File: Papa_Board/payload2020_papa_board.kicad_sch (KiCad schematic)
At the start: 18 parts, among them J2 Conn_01x05, J3 Conn_01x05_Female, J4 Conn_01x05, J5 M80-5000642, J6 M80-5000642, U11 FPF2125

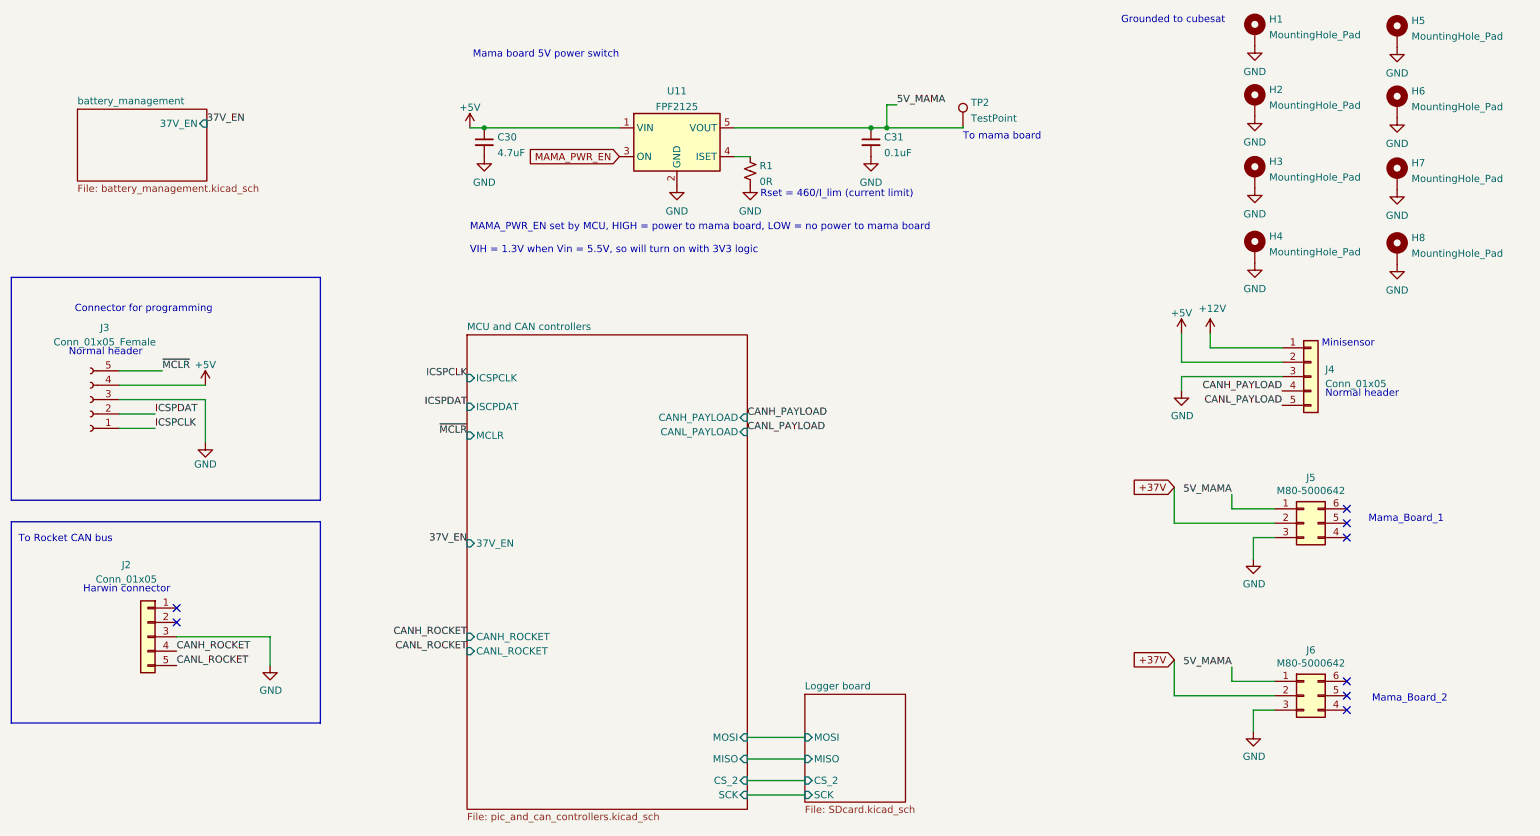
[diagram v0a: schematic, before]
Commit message: Address Jack's schematic review, still need to update PCB layout and figure out CAN connections
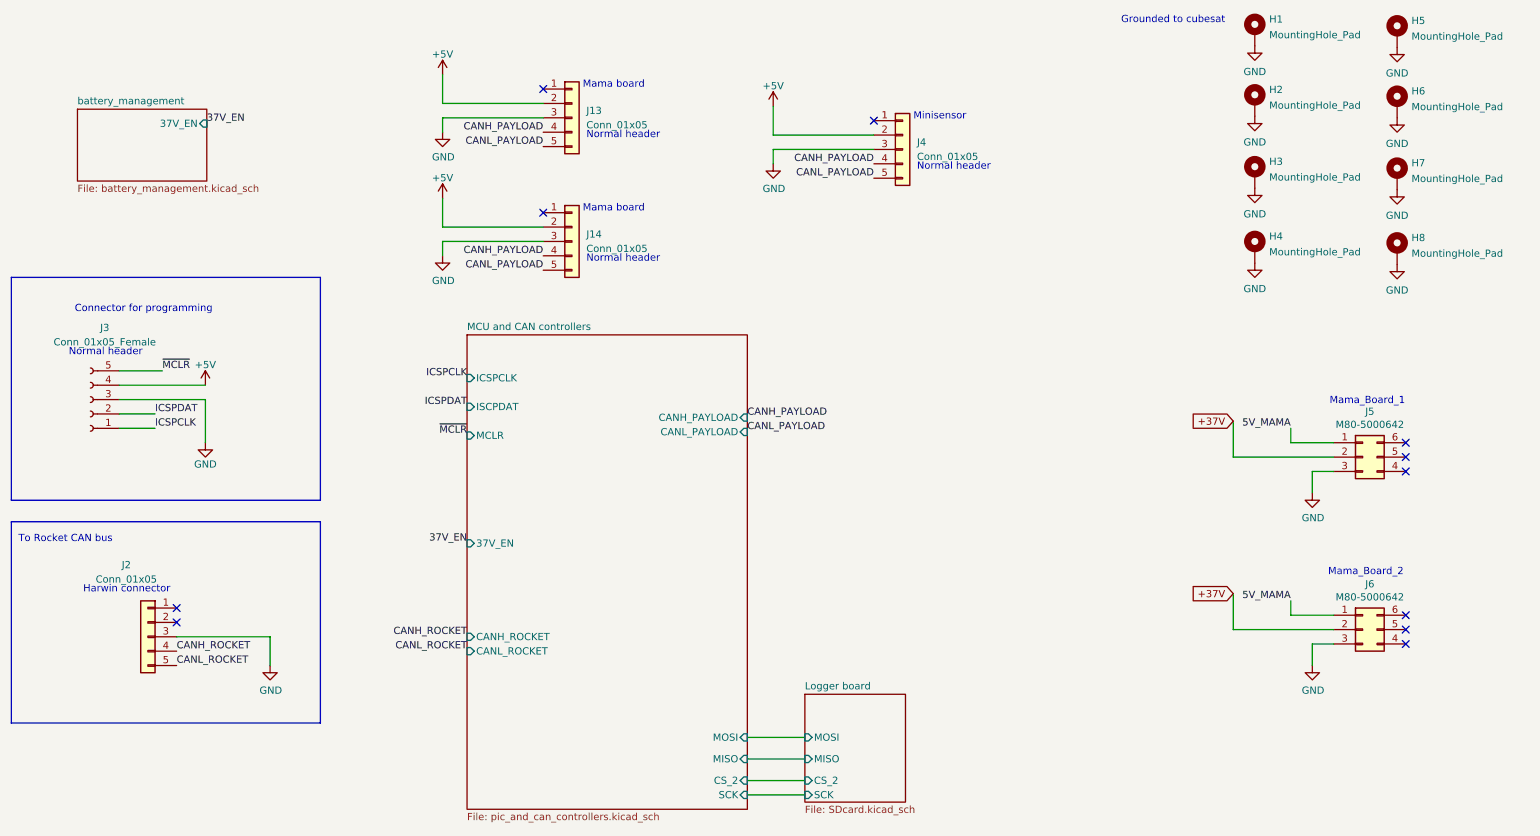
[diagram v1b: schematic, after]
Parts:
- removed C30: 4.7uF, Capacitor_SMD:C_0805_2012Metric_Pad1.18x1.45mm_HandSolder, symbol Device:C_Small
- removed C31: 0.1uF, Capacitor_SMD:C_0805_2012Metric_Pad1.18x1.45mm_HandSolder, symbol Device:C_Small
- removed R1: 0R, Resistor_SMD:R_0805_2012Metric_Pad1.20x1.40mm_HandSolder, symbol Device:R_Small_US
- removed TP2: TestPoint, Connector_PinHeader_2.54mm:PinHeader_1x01_P2.54mm_Vertical, symbol Connector:TestPoint
- removed U11: FPF2125, Package_TO_SOT_SMD:SOT-23-5_HandSoldering, symbol payload2020_custom:FPF2515
- added J13, J14: Conn_01x05, Payload2020_custom:PinHeader_2x03_P2.00mm_Vertical_MINISENSOR_Harwin_Spacing, symbol Connector_Generic:Conn_01x05
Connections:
- net +5V: now also J13.2 (Pin_2), J14.2 (Pin_2)
- net CANH_PAYLOAD: now also J13.4 (Pin_4), J14.4 (Pin_4)
- net CANL_PAYLOAD: now also J13.5 (Pin_5), J14.5 (Pin_5)
- net GND: now also J13.3 (Pin_3), J14.3 (Pin_3)
- net +12V: no longer names the net of J4.1 (Pin_1)
- no-connect marks 8 -> 11
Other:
- note added: "Mama board"
- note removed: "MAMA_PWR_EN set by MCU, HIGH = power to mama board, LOW = no power to mama board"
- note removed: "Mama board 5V power switch"
- note removed: "Rset = 460/I_lim (current limit)"
- note removed: "To mama board"
- note removed: "VIH = 1.3V when Vin = 5.5V, so will turn on with 3V3 logic"
- moved on the sheet: J4, J5, J6

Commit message: Finish PCB layout updates
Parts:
- removed J13, J14: Conn_01x05, Payload2020_custom:PinHeader_2x03_P2.00mm_Vertical_MINISENSOR_Harwin_Spacing, symbol Connector_Generic:Conn_01x05
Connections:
- no-connect marks 11 -> 9
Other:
- note removed: "Mama board"

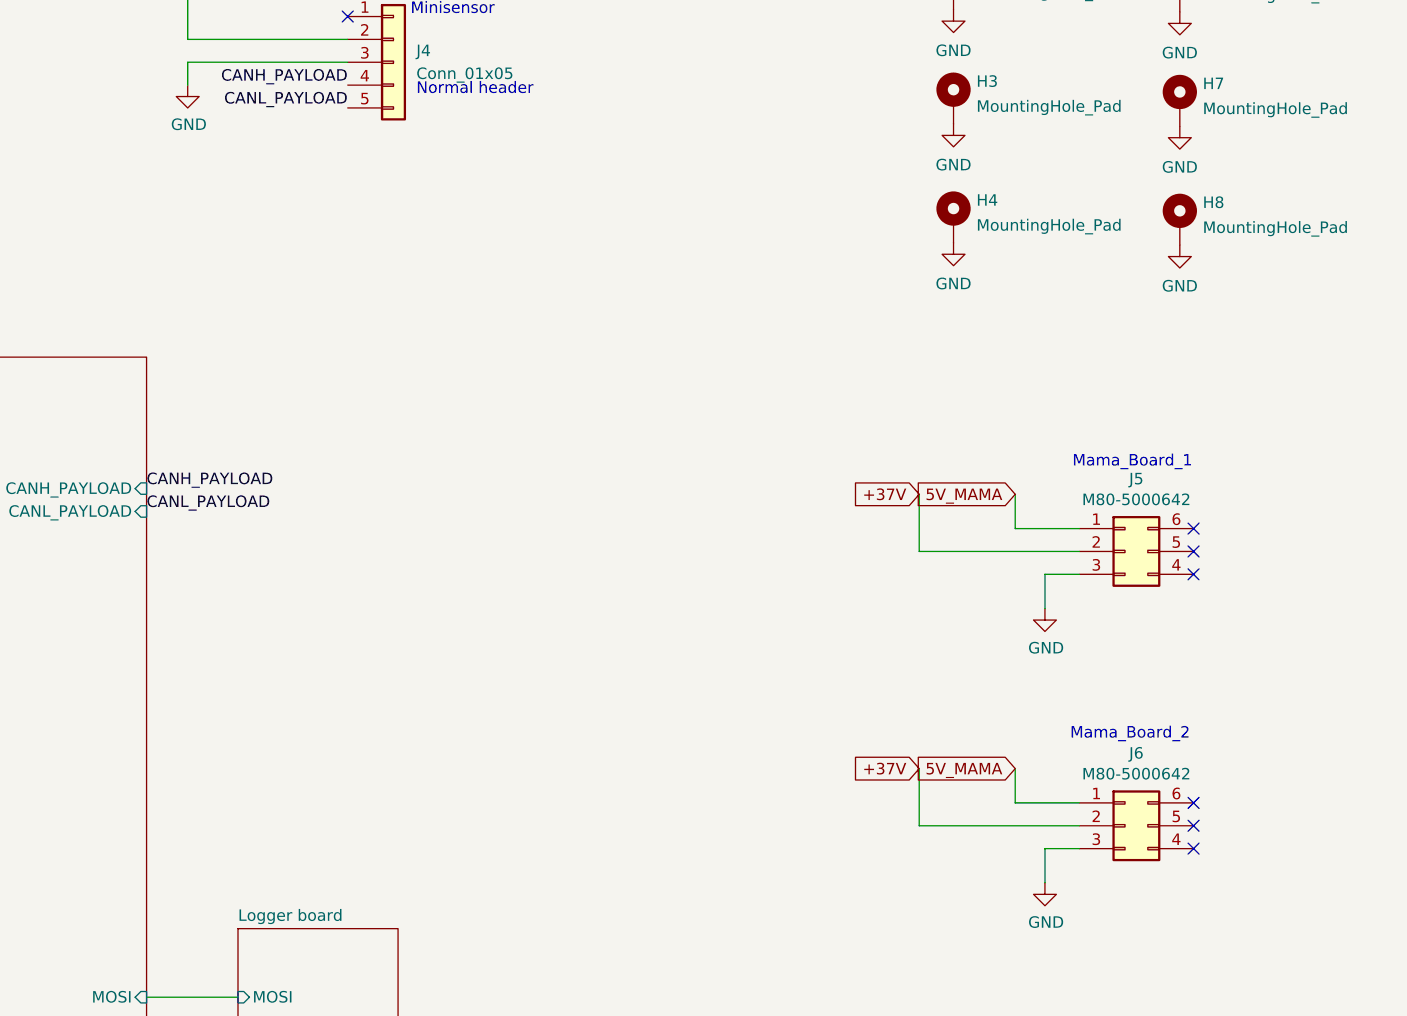
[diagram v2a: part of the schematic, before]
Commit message: Add logger board connector, CAN lines to mama board
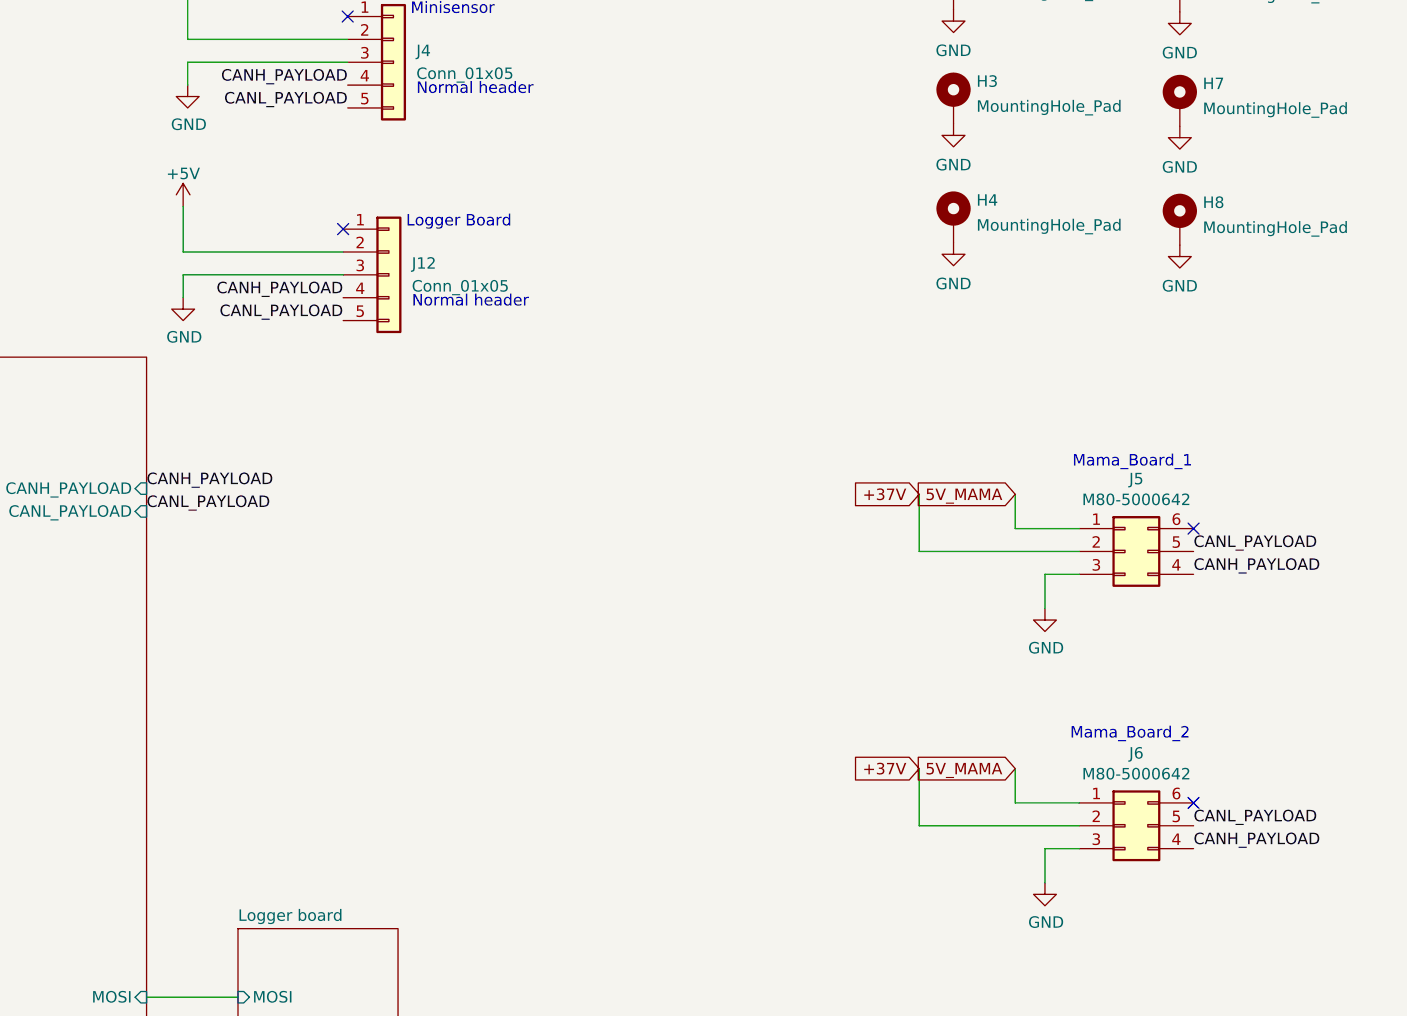
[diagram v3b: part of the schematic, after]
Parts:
- added J12: Conn_01x05, Payload2020_custom:PinHeader_2x03_P2.00mm_Vertical_MINISENSOR_Harwin_Spacing, symbol Connector_Generic:Conn_01x05
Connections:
- net +5V: now also J12.2 (Pin_2)
- net CANH_PAYLOAD: now also J5.4 (Pin_4), J6.4 (Pin_4), J12.4 (Pin_4)
- net CANL_PAYLOAD: now also J5.5 (Pin_5), J6.5 (Pin_5), J12.5 (Pin_5)
- net GND: now also J12.3 (Pin_3)
- no-connect marks 9 -> 6
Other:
- note added: "Logger Board"
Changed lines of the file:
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@@
   )
   (no_connect (at 261.874 89.154))
-  (no_connect (at 261.874 122.174))
+  (no_connect (at 167.386 55.88))
   (no_connect (at 44.704 118.364))
-  (no_connect (at 261.874 124.714))
-  (no_connect (at 261.874 94.234))
   (no_connect (at 261.874 119.634))
   (no_connect (at 167.894 32.258))
-  (no_connect (at 261.874 91.694))
   (no_connect (at 44.704 120.904))
   (wire (pts (xy 34.544 76.454) (xy 42.164 76.454))
@@
     (stroke (width 0) (type default) (color 0 0 0 0))
   )
+  (wire (pts (xy 149.606 60.96) (xy 167.386 60.96))
+    (stroke (width 0) (type default) (color 0 0 0 0))
+  )
   (wire (pts (xy 167.894 34.798) (xy 150.114 34.798))
     (stroke (width 0) (type default) (color 0 0 0 0))
@@
     (stroke (width 0) (type default) (color 0 0 0 0))
   )
+  (wire (pts (xy 167.386 58.42) (xy 149.606 58.42))
+    (stroke (width 0) (type default) (color 0 0 0 0))
+  )
   (wire (pts (xy 61.214 123.444) (xy 61.214 128.524))
     (stroke (width 0) (type default) (color 0 0 0 0))
@@
     (stroke (width 0) (type default) (color 0 0 0 0))
   )
+  (wire (pts (xy 149.606 63.5) (xy 149.606 60.96))
+    (stroke (width 0) (type default) (color 0 0 0 0))
+  )
   (polyline (pts (xy 70.104 99.314) (xy 70.104 59.944))
     (stroke (width 0) (type default) (color 0 0 0 0))
@@
   )
   (wire (pts (xy 145.542 148.844) (xy 155.702 148.844))
+    (stroke (width 0) (type default) (color 0 0 0 0))
+  )
+  (wire (pts (xy 149.606 58.42) (xy 149.606 53.34))
     (stroke (width 0) (type default) (color 0 0 0 0))
   )
@@
     (effects (font (size 1.27 1.27)) (justify left bottom))
   )
+  (text "Normal header" (at 175.006 64.77 0)
+    (effects (font (size 1.27 1.27)) (justify left bottom))
+  )
+  (text "\nLogger Board" (at 174.371 55.88 0)
+    (effects (font (size 1.27 1.27)) (justify left bottom))
+  )
   (text "\nMinisensor" (at 174.879 32.258 0)
     (effects (font (size 1.27 1.27)) (justify left bottom))
@@
     (effects (font (size 1.27 1.27)) (justify right bottom))
   )
+  (label "CANL_PAYLOAD" (at 261.874 122.174 0)
+    (effects (font (size 1.27 1.27)) (justify left bottom))
+  )
   (label "CANL_ROCKET" (at 44.704 128.524 0)
     (effects (font (size 1.27 1.27)) (justify left bottom))
@@
     (effects (font (size 1.27 1.27)) (justify right bottom))
   )
+  (label "CANH_PAYLOAD" (at 145.542 84.709 0)
+    (effects (font (size 1.27 1.27)) (justify left bottom))
+  )
+  (label "CANH_PAYLOAD" (at 261.874 94.234 0)
+    (effects (font (size 1.27 1.27)) (justify left bottom))
+  )
   (label "CANL_ROCKET" (at 96.012 125.984 180)
     (effects (font (size 1.27 1.27)) (justify right bottom))
   )
-  (label "CANL_PAYLOAD" (at 145.542 87.249 0)
-    (effects (font (size 1.27 1.27)) (justify left bottom))
+  (label "CANH_PAYLOAD" (at 167.386 63.5 180)
+    (effects (font (size 1.27 1.27)) (justify right bottom))
   )
   (label "CANL_PAYLOAD" (at 167.894 42.418 180)
     (effects (font (size 1.27 1.27)) (justify right bottom))
   )
+  (label "CANL_PAYLOAD" (at 145.542 87.249 0)
+    (effects (font (size 1.27 1.27)) (justify left bottom))
+  )
+  (label "CANL_PAYLOAD" (at 261.874 91.694 0)
+    (effects (font (size 1.27 1.27)) (justify left bottom))
+  )
+  (label "CANL_PAYLOAD" (at 167.386 66.04 180)
+    (effects (font (size 1.27 1.27)) (justify right bottom))
+  )
   (label "~{MCLR}" (at 96.012 87.884 180)
     (effects (font (size 1.27 1.27)) (justify right bottom))
   )
-  (label "CANH_PAYLOAD" (at 145.542 84.709 0)
-    (effects (font (size 1.27 1.27)) (justify left bottom))
-  )
   (label "ICSPCLK" (at 40.894 86.614 0)
     (effects (font (size 1.27 1.27)) (justify left bottom))
@@
   (label "CANH_ROCKET" (at 96.012 123.444 180)
     (effects (font (size 1.27 1.27)) (justify right bottom))
+  )
+  (label "CANH_PAYLOAD" (at 261.874 124.714 0)
+    (effects (font (size 1.27 1.27)) (justify left bottom))
   )
   (label "CANH_ROCKET" (at 44.704 125.984 0)
@@
     (pin "1")
   )
+  (symbol (lib_id "Connector_Generic:Conn_01x05") (at 172.466 60.96 0) (unit 1)
+    (in_bom yes) (on_board yes)
+    (property "Reference" "J12" (id 0) (at 175.006 59.69 0)
+      (effects (font (size 1.27 1.27)) (justify left))
+    )
+    (property "Value" "Conn_01x05" (id 1) (at 175.006 62.23 0)
+      (effects (font (size 1.27 1.27)) (justify left))
+    )
+    (property "Footprint" "Payload2020_custom:PinHeader_2x03_P2.00mm_Vertical_MINISENSOR_Harwin_Spacing" (id 2) (at 172.466 60.96 0)
+      (effects (font (size 1.27 1.27)) hide)
+    )
+    (property "Datasheet" "~" (id 3) (at 172.466 60.96 0)
+      (effects (font (size 1.27 1.27)) hide)
+    )
+    (pin "1")
+    (pin "2")
+    (pin "3")
+    (pin "4")
+    (pin "5")
+  )
   (symbol (lib_id "power:GND") (at 260.35 44.45 0) (unit 1)
     (in_bom yes) (on_board yes) (fields_autoplaced)
@@
     )
     (property "Datasheet" "" (id 3) (at 260.35 19.304 0)
+      (effects (font (size 1.27 1.27)) hide)
+    )
+    (pin "1")
+  )
+  (symbol (lib_id "power:+5V") (at 149.606 53.34 0) (unit 1)
+    (in_bom yes) (on_board yes) (fields_autoplaced)
+    (property "Reference" "#PWR0103" (id 0) (at 149.606 57.15 0)
+      (effects (font (size 1.27 1.27)) hide)
+    )
+    (property "Value" "+5V" (id 1) (at 149.606 49.7355 0))
+    (property "Footprint" "" (id 2) (at 149.606 53.34 0)
+      (effects (font (size 1.27 1.27)) hide)
+    )
+    (property "Datasheet" "" (id 3) (at 149.606 53.34 0)
+      (effects (font (size 1.27 1.27)) hide)
+    )
+    (pin "1")
+  )
+  (symbol (lib_id "power:GND") (at 149.606 63.5 0) (unit 1)
+    (in_bom yes) (on_board yes)
+    (property "Reference" "#PWR0102" (id 0) (at 149.606 69.85 0)
+      (effects (font (size 1.27 1.27)) hide)
+    )
+    (property "Value" "GND" (id 1) (at 149.733 67.8942 0))
+    (property "Footprint" "" (id 2) (at 149.606 63.5 0)
+      (effects (font (size 1.27 1.27)) hide)
+    )
+    (property "Datasheet" "" (id 3) (at 149.606 63.5 0)
       (effects (font (size 1.27 1.27)) hide)
     )
@@
       (reference "#PWR016") (unit 1) (value "GND") (footprint "")
     )
-    (path "/00000000-0000-0000-0000-00005e13f8e9/fa532ef2-9df3-48eb-a505-4d84c8854573"
-      (reference "#PWR017") (unit 1) (value "+3.3V") (footprint "")
-    )
     (path "/00000000-0000-0000-0000-00006016c5cd/00000000-0000-0000-0000-000060adfb63"
       (reference "#PWR018") (unit 1) (value "GND") (footprint "")
@@
       (reference "#PWR020") (unit 1) (value "GND") (footprint "")
     )
-    (path "/00000000-0000-0000-0000-00005e13f8e9/f8a31230-9132-48e5-be60-966a75847863"
-      (reference "#PWR021") (unit 1) (value "+5V") (footprint "")
-    )
     (path "/00000000-0000-0000-0000-000060a2c79f/cbae823c-c057-4973-bce2-ef3dccaf1363"
       (reference "#PWR022") (unit 1) (value "+3.3V") (footprint "")
@@
       (reference "#PWR0101") (unit 1) (value "+3.3V") (footprint "")
     )
+    (path "/b5bfa1f3-6fd3-434b-9124-e1b761db6154"
+      (reference "#PWR0102") (unit 1) (value "GND") (footprint "")
+    )
+    (path "/91bd653c-baf8-410c-a9e5-0f265bb01cd1"
+      (reference "#PWR0103") (unit 1) (value "+5V") (footprint "")
+    )
     (path "/00000000-0000-0000-0000-00005e13f8e9/9f4a3db1-836b-43f0-ac94-ad1e6d923354"
       (reference "#PWR0104") (unit 1) (value "GND") (footprint "")
@@
       (reference "J11") (unit 1) (value "GND TEST CONN") (footprint "Connector_PinHeader_2.54mm:PinHeader_1x02_P2.54mm_Vertical")
     )
-    (path "/00000000-0000-0000-0000-00005e13f8e9/c74fb210-1c47-48ae-98cb-eb5f6ad14759"
-      (reference "J12") (unit 1) (value "VOLTAGE TEST CONN") (footprint "Connector_PinHeader_2.54mm:PinHeader_1x06_P2.54mm_Vertical")
+    (path "/6d7f2f1f-cc6f-4b13-b99d-97ea8390d298"
+      (reference "J12") (unit 1) (value "Conn_01x05") (footprint "Payload2020_custom:PinHeader_2x03_P2.00mm_Vertical_MINISENSOR_Harwin_Spacing")
     )
     (path "/00000000-0000-0000-0000-00005e13f8e9/00000000-0000-0000-0000-000060b36838"

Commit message: made last fixes & revision, generated gerbers
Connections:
- net +5V: now also J12.4 (Pin_4); no longer J12.2 (Pin_2), J3.4 (Pin_4)
- net CANH_PAYLOAD: now also J12.2 (Pin_2); no longer J12.4 (Pin_4)
- net CANL_PAYLOAD: now also J12.1 (Pin_1); no longer J12.5 (Pin_5)
- new net +3V3: J3.4 (Pin_4)
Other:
- moved on the sheet: J3
